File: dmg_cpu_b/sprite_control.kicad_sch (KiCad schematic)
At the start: 106 parts

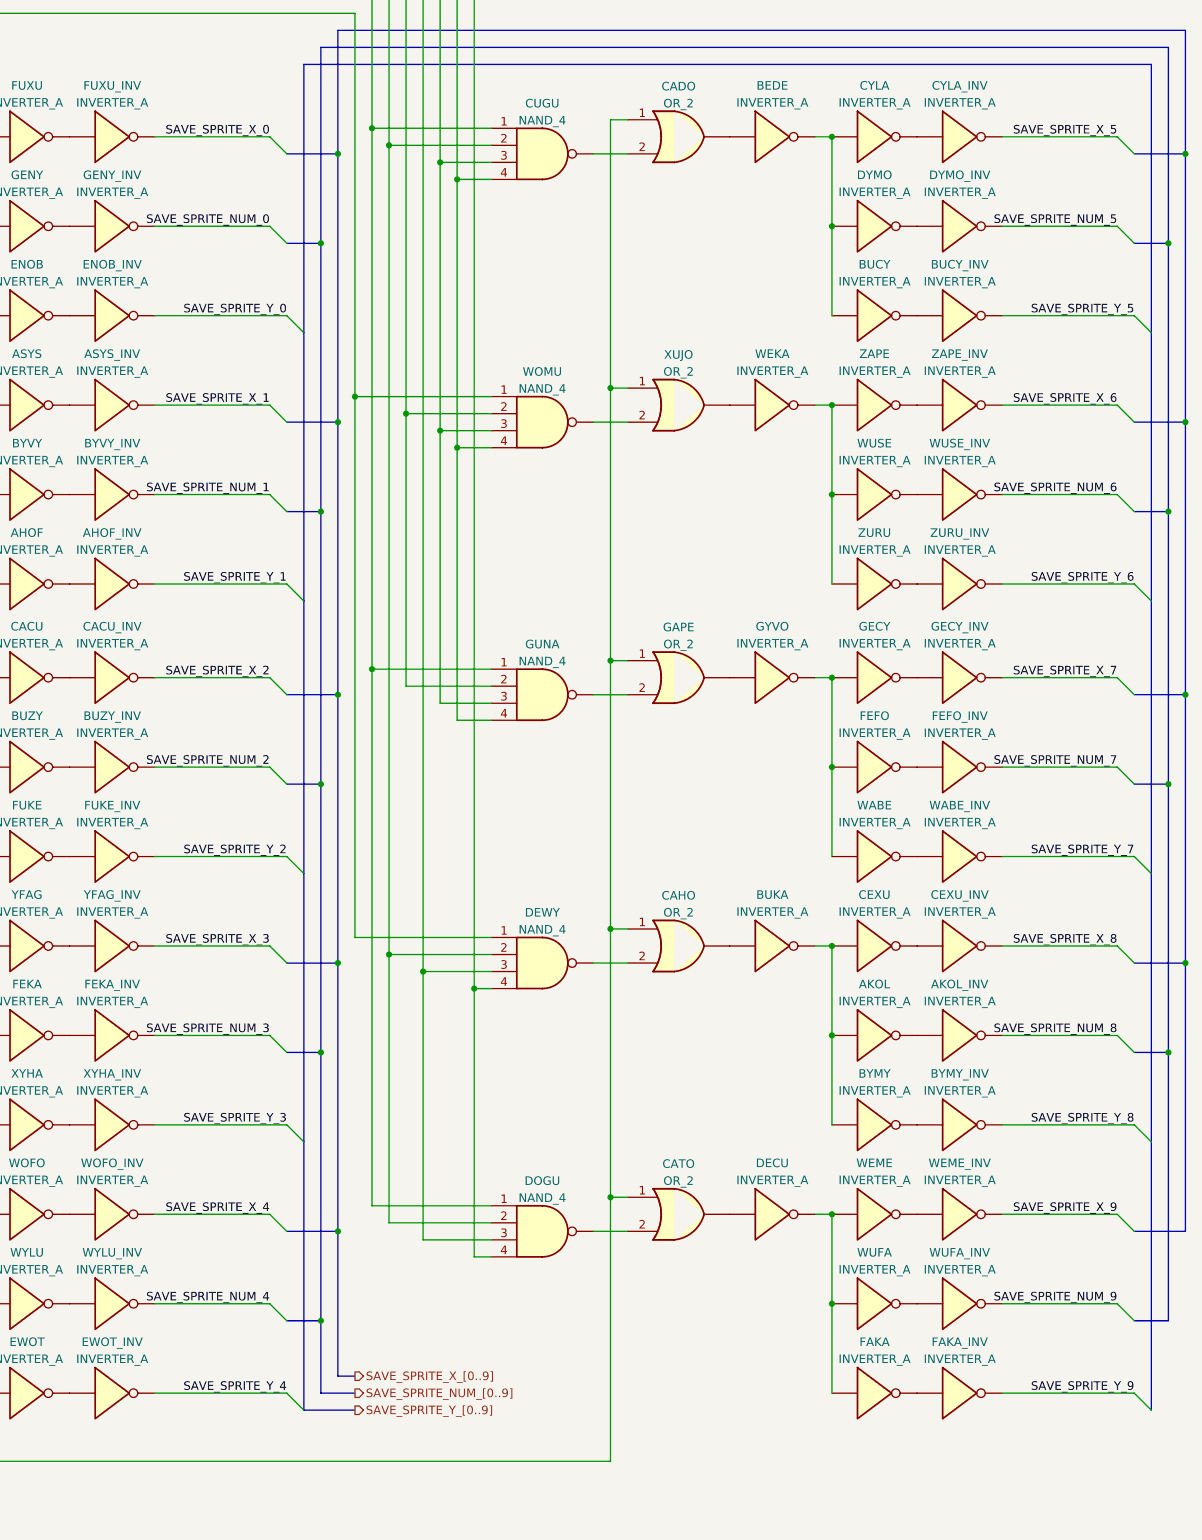
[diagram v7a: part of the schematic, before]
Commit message: Quite a few fixes from review.
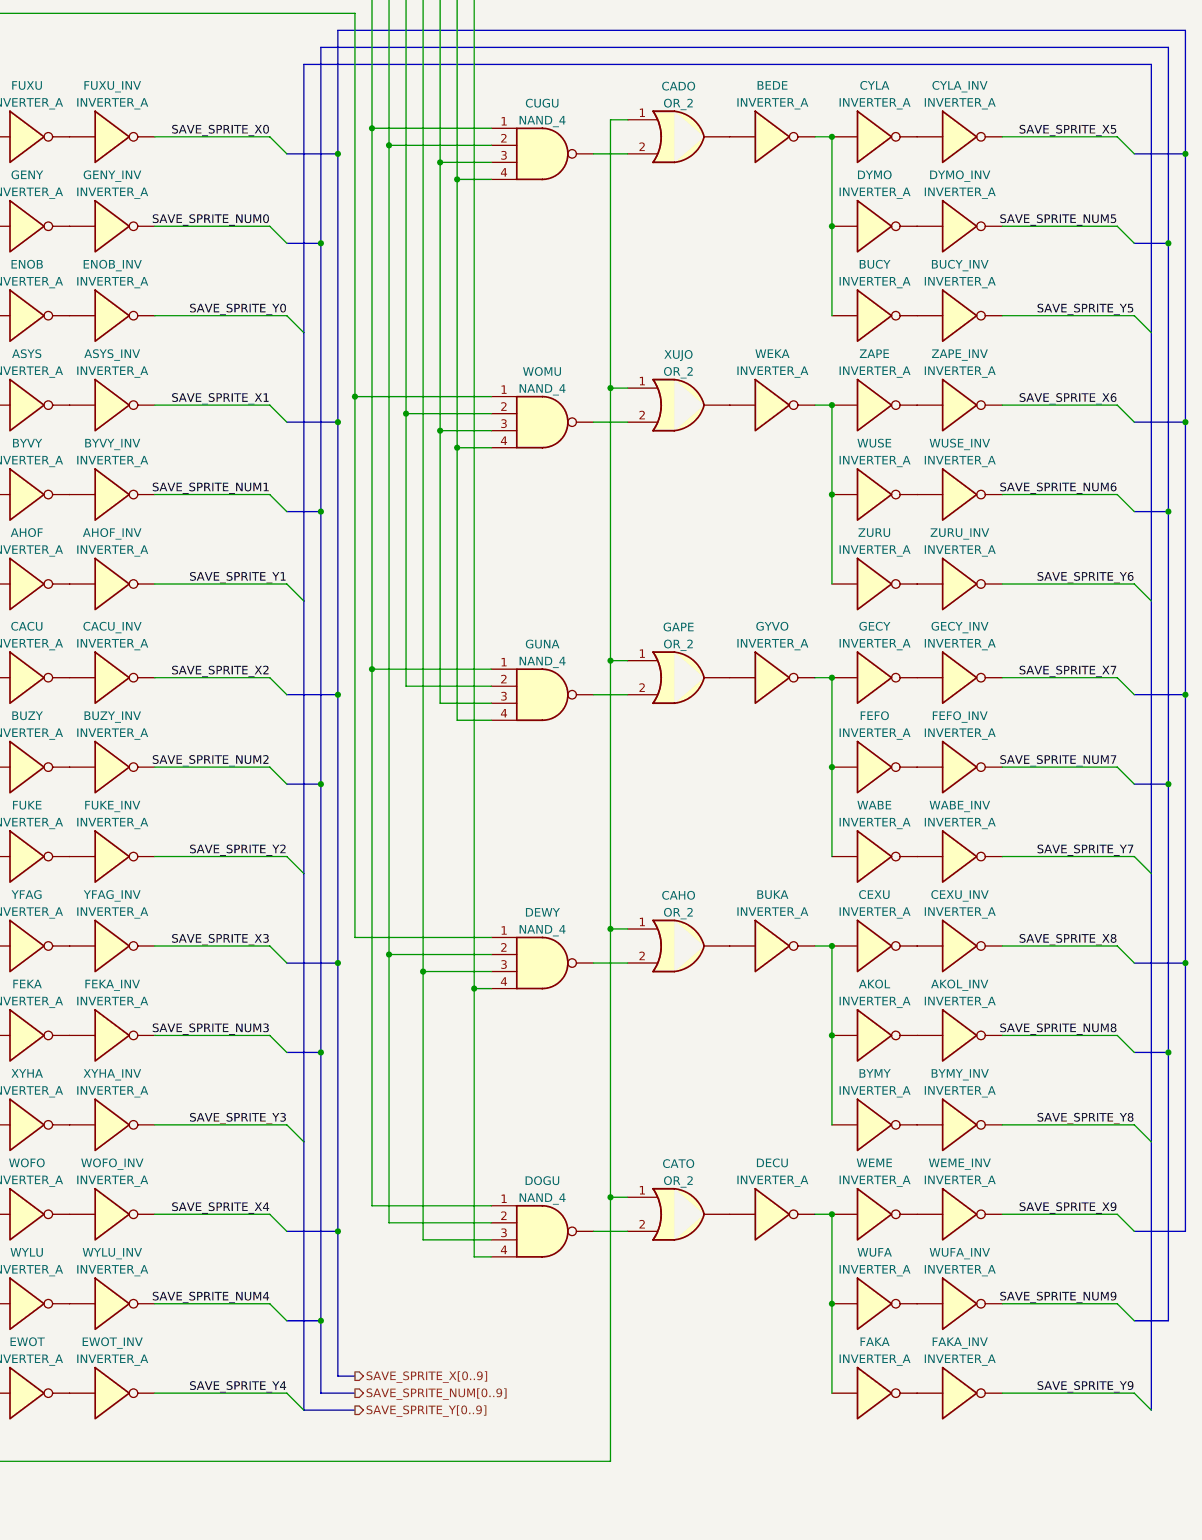
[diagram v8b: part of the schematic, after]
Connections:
- net SAVE_SPRITE_NUM_0 renamed SAVE_SPRITE_NUM0
- net SAVE_SPRITE_NUM_1 renamed SAVE_SPRITE_NUM1
- net SAVE_SPRITE_NUM_2 renamed SAVE_SPRITE_NUM2
- net SAVE_SPRITE_NUM_3 renamed SAVE_SPRITE_NUM3
- net SAVE_SPRITE_NUM_4 renamed SAVE_SPRITE_NUM4
- net SAVE_SPRITE_NUM_5 renamed SAVE_SPRITE_NUM5
- net SAVE_SPRITE_NUM_6 renamed SAVE_SPRITE_NUM6
- net SAVE_SPRITE_NUM_7 renamed SAVE_SPRITE_NUM7
- net SAVE_SPRITE_NUM_8 renamed SAVE_SPRITE_NUM8
- net SAVE_SPRITE_NUM_9 renamed SAVE_SPRITE_NUM9
- net SAVE_SPRITE_X_0 renamed SAVE_SPRITE_X0
- net SAVE_SPRITE_X_1 renamed SAVE_SPRITE_X1
- net SAVE_SPRITE_X_2 renamed SAVE_SPRITE_X2
- net SAVE_SPRITE_X_3 renamed SAVE_SPRITE_X3
- net SAVE_SPRITE_X_4 renamed SAVE_SPRITE_X4
- net SAVE_SPRITE_X_5 renamed SAVE_SPRITE_X5
- net SAVE_SPRITE_X_6 renamed SAVE_SPRITE_X6
- net SAVE_SPRITE_X_7 renamed SAVE_SPRITE_X7
- net SAVE_SPRITE_X_8 renamed SAVE_SPRITE_X8
- net SAVE_SPRITE_X_9 renamed SAVE_SPRITE_X9
- net SAVE_SPRITE_Y_0 renamed SAVE_SPRITE_Y0
- net SAVE_SPRITE_Y_1 renamed SAVE_SPRITE_Y1
- net SAVE_SPRITE_Y_2 renamed SAVE_SPRITE_Y2
- net SAVE_SPRITE_Y_3 renamed SAVE_SPRITE_Y3
- net SAVE_SPRITE_Y_4 renamed SAVE_SPRITE_Y4
- net SAVE_SPRITE_Y_5 renamed SAVE_SPRITE_Y5
- net SAVE_SPRITE_Y_6 renamed SAVE_SPRITE_Y6
- net SAVE_SPRITE_Y_7 renamed SAVE_SPRITE_Y7
- net SAVE_SPRITE_Y_8 renamed SAVE_SPRITE_Y8
- net SAVE_SPRITE_Y_9 renamed SAVE_SPRITE_Y9
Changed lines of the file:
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@@
     (effects (font (size 1.27 1.27)) (justify left bottom))
   )
-  (label "SAVE_SPRITE_NUM_0" (at 269.24 66.04 180)
+  (label "SAVE_SPRITE_NUM0" (at 269.24 66.04 180)
     (effects (font (size 1.27 1.27)) (justify right bottom))
   )
-  (label "SAVE_SPRITE_NUM_8" (at 395.605 186.69 180)
+  (label "SAVE_SPRITE_NUM8" (at 395.605 186.69 180)
     (effects (font (size 1.27 1.27)) (justify right bottom))
   )
-  (label "SAVE_SPRITE_X_4" (at 269.24 213.36 180)
+  (label "SAVE_SPRITE_X4" (at 269.24 213.36 180)
     (effects (font (size 1.27 1.27)) (justify right bottom))
   )
-  (label "SAVE_SPRITE_Y_3" (at 271.78 200.025 180)
+  (label "SAVE_SPRITE_Y3" (at 271.78 200.025 180)
     (effects (font (size 1.27 1.27)) (justify right bottom))
   )
-  (label "SAVE_SPRITE_X_0" (at 269.24 52.705 180)
+  (label "SAVE_SPRITE_X0" (at 269.24 52.705 180)
     (effects (font (size 1.27 1.27)) (justify right bottom))
   )
-  (label "SAVE_SPRITE_Y_2" (at 271.78 160.02 180)
+  (label "SAVE_SPRITE_Y2" (at 271.78 160.02 180)
     (effects (font (size 1.27 1.27)) (justify right bottom))
   )
-  (label "SAVE_SPRITE_NUM_9" (at 395.605 226.695 180)
+  (label "SAVE_SPRITE_NUM9" (at 395.605 226.695 180)
     (effects (font (size 1.27 1.27)) (justify right bottom))
   )
-  (label "SAVE_SPRITE_NUM_1" (at 269.24 106.045 180)
+  (label "SAVE_SPRITE_NUM1" (at 269.24 106.045 180)
     (effects (font (size 1.27 1.27)) (justify right bottom))
   )
-  (label "SAVE_SPRITE_Y_1" (at 271.78 119.38 180)
+  (label "SAVE_SPRITE_Y1" (at 271.78 119.38 180)
     (effects (font (size 1.27 1.27)) (justify right bottom))
   )
-  (label "SAVE_SPRITE_X_2" (at 269.24 133.35 180)
+  (label "SAVE_SPRITE_X2" (at 269.24 133.35 180)
     (effects (font (size 1.27 1.27)) (justify right bottom))
   )
-  (label "SAVE_SPRITE_X_5" (at 395.605 52.705 180)
+  (label "SAVE_SPRITE_X5" (at 395.605 52.705 180)
     (effects (font (size 1.27 1.27)) (justify right bottom))
   )
-  (label "SAVE_SPRITE_NUM_6" (at 395.605 106.045 180)
+  (label "SAVE_SPRITE_NUM6" (at 395.605 106.045 180)
     (effects (font (size 1.27 1.27)) (justify right bottom))
   )
-  (label "SAVE_SPRITE_NUM_7" (at 395.605 146.685 180)
+  (label "SAVE_SPRITE_NUM7" (at 395.605 146.685 180)
     (effects (font (size 1.27 1.27)) (justify right bottom))
   )
-  (label "SAVE_SPRITE_NUM_4" (at 269.24 226.695 180)
+  (label "SAVE_SPRITE_NUM4" (at 269.24 226.695 180)
     (effects (font (size 1.27 1.27)) (justify right bottom))
   )
-  (label "SAVE_SPRITE_Y_9" (at 398.145 240.03 180)
+  (label "SAVE_SPRITE_Y9" (at 398.145 240.03 180)
     (effects (font (size 1.27 1.27)) (justify right bottom))
   )
-  (label "SAVE_SPRITE_X_6" (at 395.605 92.71 180)
+  (label "SAVE_SPRITE_X6" (at 395.605 92.71 180)
     (effects (font (size 1.27 1.27)) (justify right bottom))
   )
-  (label "SAVE_SPRITE_X_8" (at 395.605 173.355 180)
+  (label "SAVE_SPRITE_X8" (at 395.605 173.355 180)
     (effects (font (size 1.27 1.27)) (justify right bottom))
   )
-  (label "SAVE_SPRITE_NUM_3" (at 269.24 186.69 180)
+  (label "SAVE_SPRITE_NUM3" (at 269.24 186.69 180)
     (effects (font (size 1.27 1.27)) (justify right bottom))
   )
-  (label "SAVE_SPRITE_X_7" (at 395.605 133.35 180)
+  (label "SAVE_SPRITE_X7" (at 395.605 133.35 180)
     (effects (font (size 1.27 1.27)) (justify right bottom))
   )
-  (label "SAVE_SPRITE_Y_6" (at 398.145 119.38 180)
+  (label "SAVE_SPRITE_Y6" (at 398.145 119.38 180)
     (effects (font (size 1.27 1.27)) (justify right bottom))
   )
-  (label "SAVE_SPRITE_Y_8" (at 398.145 200.025 180)
+  (label "SAVE_SPRITE_Y8" (at 398.145 200.025 180)
     (effects (font (size 1.27 1.27)) (justify right bottom))
   )
-  (label "SAVE_SPRITE_X_1" (at 269.24 92.71 180)
+  (label "SAVE_SPRITE_X1" (at 269.24 92.71 180)
     (effects (font (size 1.27 1.27)) (justify right bottom))
   )
-  (label "SAVE_SPRITE_Y_0" (at 271.78 79.375 180)
+  (label "SAVE_SPRITE_Y0" (at 271.78 79.375 180)
     (effects (font (size 1.27 1.27)) (justify right bottom))
   )
-  (label "SAVE_SPRITE_X_3" (at 269.24 173.355 180)
+  (label "SAVE_SPRITE_X3" (at 269.24 173.355 180)
     (effects (font (size 1.27 1.27)) (justify right bottom))
   )
-  (label "SAVE_SPRITE_Y_7" (at 398.145 160.02 180)
+  (label "SAVE_SPRITE_Y7" (at 398.145 160.02 180)
     (effects (font (size 1.27 1.27)) (justify right bottom))
   )
-  (label "SAVE_SPRITE_NUM_5" (at 395.605 66.04 180)
+  (label "SAVE_SPRITE_NUM5" (at 395.605 66.04 180)
     (effects (font (size 1.27 1.27)) (justify right bottom))
   )
-  (label "SAVE_SPRITE_NUM_2" (at 269.24 146.685 180)
+  (label "SAVE_SPRITE_NUM2" (at 269.24 146.685 180)
     (effects (font (size 1.27 1.27)) (justify right bottom))
   )
-  (label "SAVE_SPRITE_Y_4" (at 271.78 240.03 180)
+  (label "SAVE_SPRITE_Y4" (at 271.78 240.03 180)
     (effects (font (size 1.27 1.27)) (justify right bottom))
   )
-  (label "SAVE_SPRITE_X_9" (at 395.605 213.36 180)
+  (label "SAVE_SPRITE_X9" (at 395.605 213.36 180)
     (effects (font (size 1.27 1.27)) (justify right bottom))
   )
-  (label "SAVE_SPRITE_Y_5" (at 398.145 79.375 180)
+  (label "SAVE_SPRITE_Y5" (at 398.145 79.375 180)
     (effects (font (size 1.27 1.27)) (justify right bottom))
   )
-  (hierarchical_label "SAVE_SPRITE_NUM_[0..9]" (shape output) (at 281.94 240.03 0)
+  (hierarchical_label "SAVE_SPRITE_NUM[0..9]" (shape output) (at 281.94 240.03 0)
     (effects (font (size 1.27 1.27)) (justify left))
   )
@@
     (effects (font (size 1.27 1.27)) (justify right))
   )
-  (hierarchical_label "SAVE_SPRITE_X_[0..9]" (shape output) (at 281.94 237.49 0)
+  (hierarchical_label "SAVE_SPRITE_X[0..9]" (shape output) (at 281.94 237.49 0)
     (effects (font (size 1.27 1.27)) (justify left))
   )
@@
     (effects (font (size 1.27 1.27)) (justify right))
   )
-  (hierarchical_label "SAVE_SPRITE_Y_[0..9]" (shape output) (at 281.94 242.57 0)
+  (hierarchical_label "SAVE_SPRITE_Y[0..9]" (shape output) (at 281.94 242.57 0)
     (effects (font (size 1.27 1.27)) (justify left))
   )
